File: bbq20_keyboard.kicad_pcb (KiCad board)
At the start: 2 copper layers, 74 x 53.1 mm, 103 parts, among them J1 Conn_Stemma_QT, J2 PMOD, J3 USB_C_Receptacle_USB2.0, Q1 BSS138, Q2 BSS138, Q3 BSS138, Q4 BSS138, Q5 BSS138, Q6 BSS138, U1 RP2040, U2 AP2112K-3.3, U3 GD25Q16xS, U4 BBQ20KBD, U5 ME6212C18M5G, U6 ME6212C28M5G, Y1 XYDBPCNANF-12MHZ

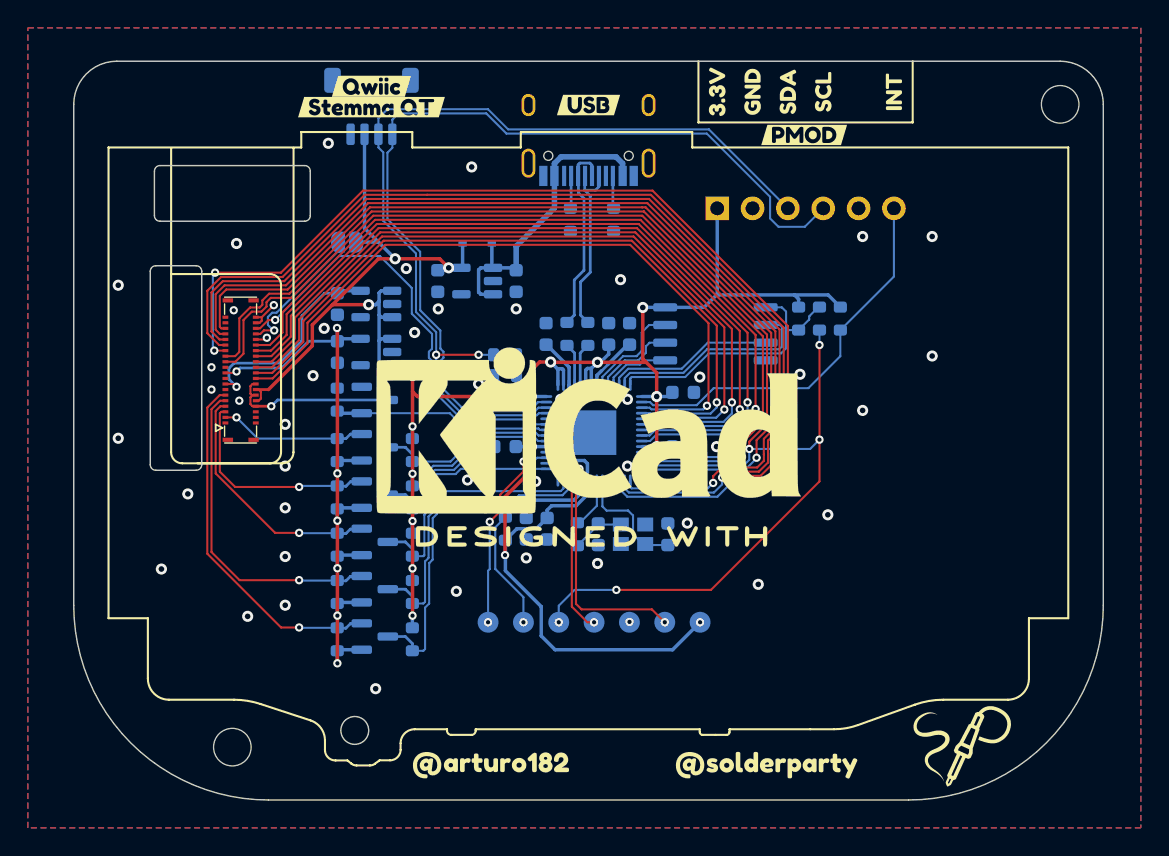
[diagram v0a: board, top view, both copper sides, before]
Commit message: Migrate KiCAD version -> 1.0, update part numbers
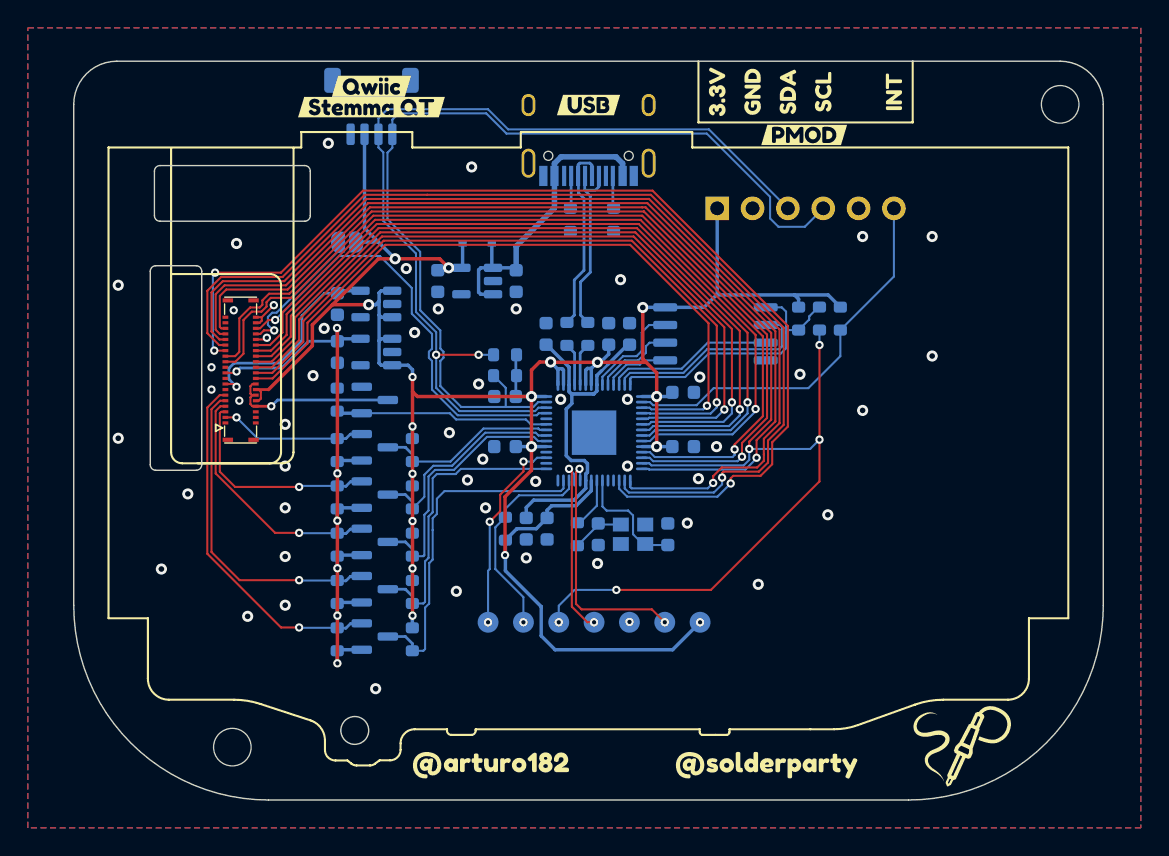
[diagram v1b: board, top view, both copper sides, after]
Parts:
- removed REF**: KiCad-Logo2_12mm_SilkScreen, Symbol:KiCad-Logo2_12mm_SilkScreen
